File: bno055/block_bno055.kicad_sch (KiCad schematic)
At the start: 11 parts, among them U1 BNO055, Y1 NX3215SA-32.768K-STD-MUA-14

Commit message: [Rushil] added block of ds3231_rtc
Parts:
- added R2, R5: 10k, Resistor_SMD:R_0603_1608Metric, symbol Library:R
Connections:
- net +3V3: now also R2.1, R5.1
- net SCL: now also R2.2
- net SDA: now also R5.2

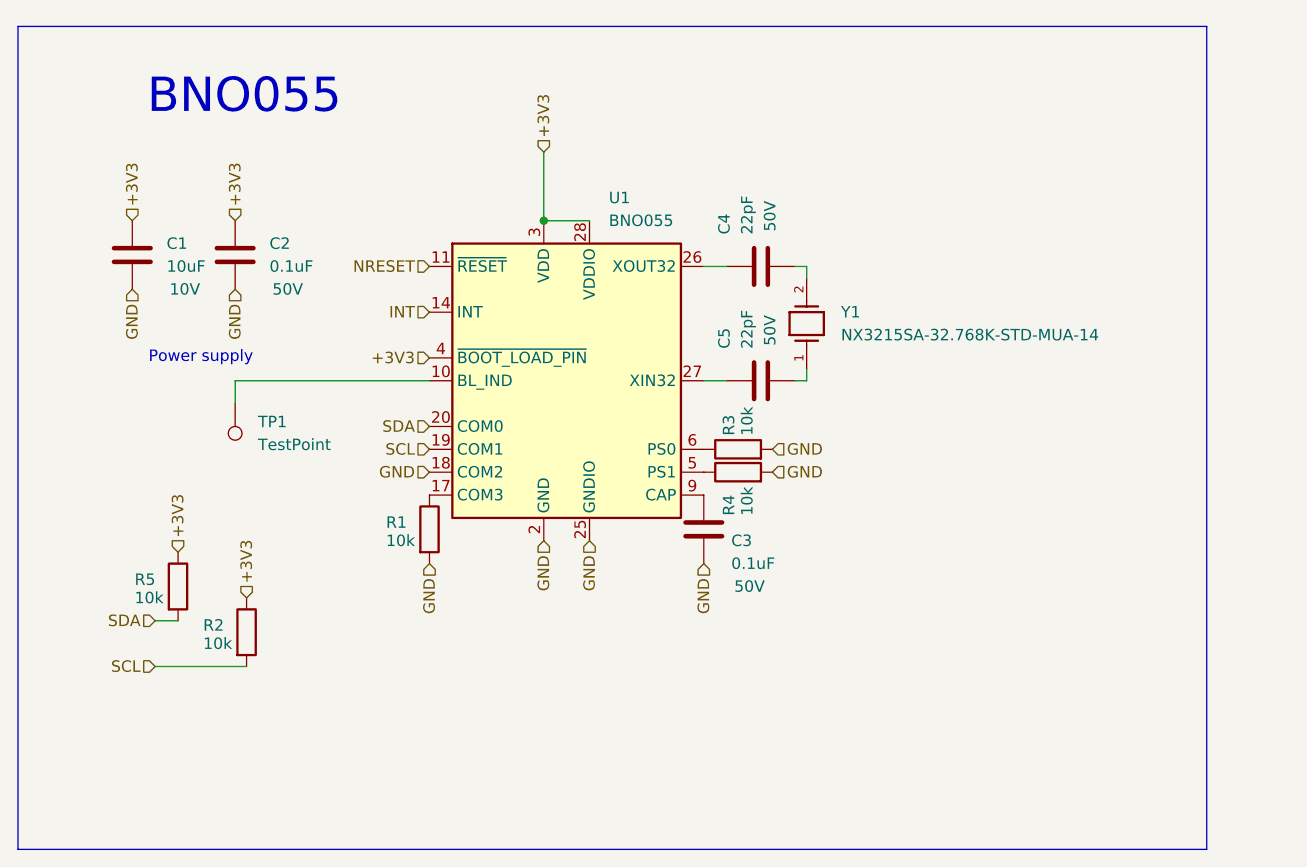
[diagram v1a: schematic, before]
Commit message: [Rushil] corrected pcb added information on both schematic and pcb user drawing correct circuit of bno055
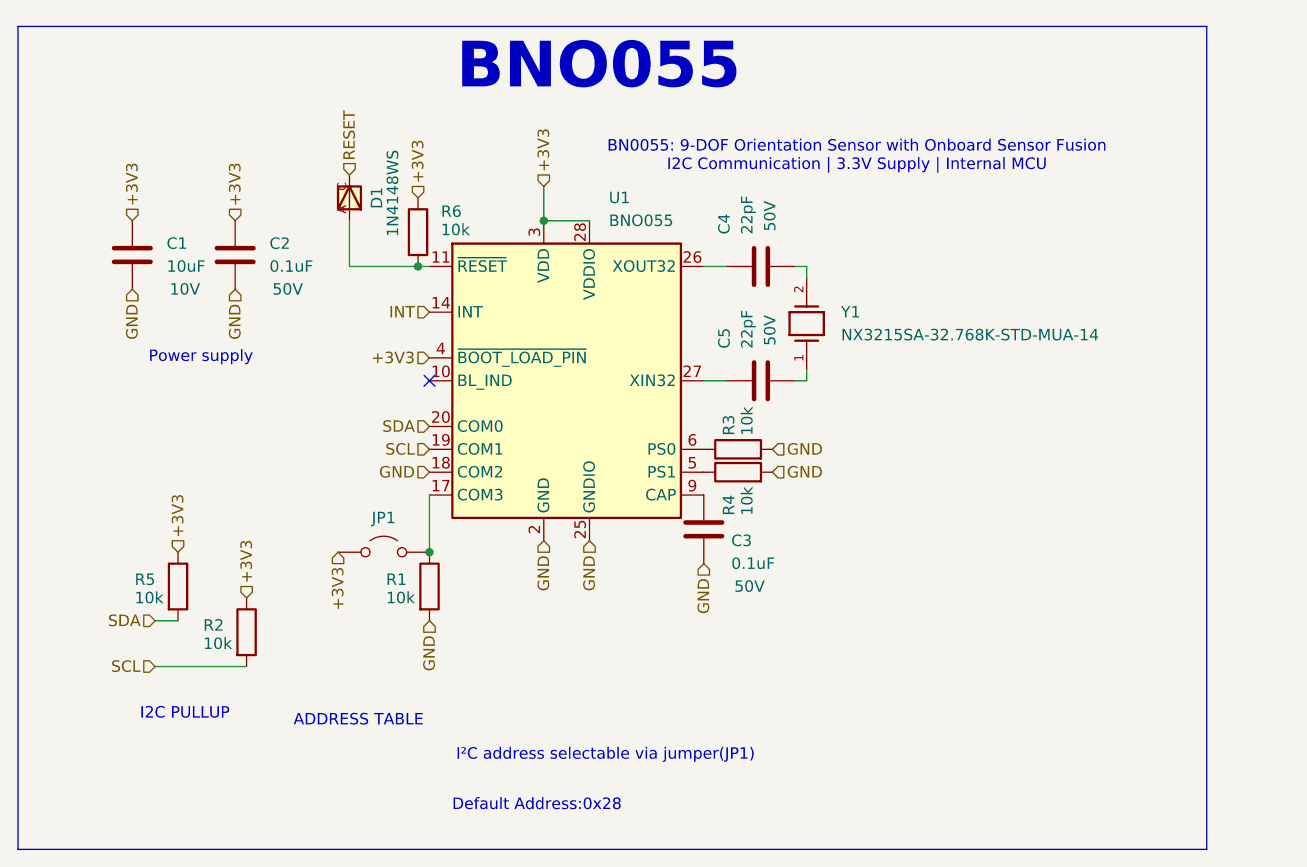
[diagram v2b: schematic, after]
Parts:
- removed TP1: TestPoint, TestPoint:TestPoint_Pad_D1.5mm, symbol Library:TestPoint
- added D1: 1N4148WS, 1N4148WS:SOD323, symbol Library:1N4148WS
- added JP1: Jumper_2_Open, Jumper:SolderJumper-2_P1.3mm_Open_RoundedPad1.0x1.5mm, symbol Library:Jumper_2_Open
- added R6: 10k, Resistor_SMD:R_0603_1608Metric, symbol Library:R
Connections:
- net +3V3: now also JP1.1 (A), R6.1
- net at R1.1, U1.17 (COM3): now also JP1.2 (B)
- net NRESET: no longer names the net of U1.11 (~{RESET})
- net NRESET: now also D1.A, R6.2
- new net RESET: D1.C
- no-connect marks 0 -> 1
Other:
- note added: "ADDRESS TABLE"
- note added: "BN0055: 9-DOF Orientation Sensor with Onboard Sensor Fusion I2C Communication | 3.3V Supply | Internal MCU"
- note added: "Default Address:0x28"
- note added: "I2C PULLUP"
- note added: "I²C address selectable via jumper(JP1)"
- moved on the sheet: R1

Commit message: [Rushil] added ams1117-3.3 block and did some clean up in schematic info part
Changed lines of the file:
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@@
 	(text "BN0055: 9-DOF Orientation Sensor with Onboard Sensor Fusion\nI2C Communication | 3.3V Supply | Internal MCU\n"
 		(exclude_from_sim no)
-		(at 180.848 67.818 0)
+		(at 155.194 67.818 0)
 		(effects
 			(font
 				(size 1.27 1.27)
 			)
+			(justify left)
 		)
 	)

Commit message: fixed BNO055
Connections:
- net +3V3 renamed 3V3
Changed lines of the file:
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@@
 	(text "Default Address:0x28\n"
 		(exclude_from_sim no)
-		(at 145.288 139.954 0)
+		(at 144.018 136.652 0)
 		(effects
 			(font
@@
 			(width 0)
 			(type default)
+		)
+	)
+	(table
+		(column_count 1)
+		(border
+			(external yes)
+			(header yes)
+			(stroke
+				(width 0)
+				(type solid)
+			)
+		)
+		(separators
+			(rows yes)
+			(cols yes)
+			(stroke
+				(width 0)
+				(type solid)
+			)
+		)
+		(column_widths 6.35)
+		(row_heights 2.54 2.54 2.54)
+		(cells
+			(table_cell "COM3"
+				(exclude_from_sim no)
+				(at 119.38 133.35 0)
+				(size 6.35 2.54)
+				(margins 0.9525 0.9525 0.9525 0.9525)
+				(span 1 1)
+				(fill
+					(type none)
+				)
+				(effects
+					(font
+						(size 1.27 1.27)
+					)
+					(justify left top)
+				)
+			)
+			(table_cell "HIGH"
+				(exclude_from_sim no)
+				(at 119.38 135.89 0)
+				(size 6.35 2.54)
+				(margins 0.9525 0.9525 0.9525 0.9525)
+				(span 1 1)
+				(fill
+					(type none)
+				)
+				(effects
+					(font
+						(size 1.27 1.27)
+					)
+					(justify left top)
+				)
+			)
+			(table_cell "LOW"
+				(exclude_from_sim no)
+				(at 119.38 138.43 0)
+				(size 6.35 2.54)
+				(margins 0.9525 0.9525 0.9525 0.9525)
+				(span 1 1)
+				(fill
+					(type none)
+				)
+				(effects
+					(font
+						(size 1.27 1.27)
+					)
+					(justify left top)
+				)
+			)
 		)
 	)
@@
 		)
 	)
-	(table
-		(column_count 1)
-		(border
-			(external yes)
-			(header yes)
-			(stroke
-				(width 0)
-				(type solid)
-			)
-		)
-		(separators
-			(rows yes)
-			(cols yes)
-			(stroke
-				(width 0)
-				(type solid)
-			)
-		)
-		(column_widths 6.35)
-		(row_heights 2.54 2.54 2.54)
-		(cells
-			(table_cell "COM3"
-				(exclude_from_sim no)
-				(at 119.38 133.35 0)
-				(size 6.35 2.54)
-				(margins 0.9525 0.9525 0.9525 0.9525)
-				(span 1 1)
-				(fill
-					(type none)
-				)
-				(effects
-					(font
-						(size 1.27 1.27)
-					)
-					(justify left top)
-				)
-			)
-			(table_cell "HIGH"
-				(exclude_from_sim no)
-				(at 119.38 135.89 0)
-				(size 6.35 2.54)
-				(margins 0.9525 0.9525 0.9525 0.9525)
-				(span 1 1)
-				(fill
-					(type none)
-				)
-				(effects
-					(font
-						(size 1.27 1.27)
-					)
-					(justify left top)
-				)
-			)
-			(table_cell "LOW"
-				(exclude_from_sim no)
-				(at 119.38 138.43 0)
-				(size 6.35 2.54)
-				(margins 0.9525 0.9525 0.9525 0.9525)
-				(span 1 1)
-				(fill
-					(type none)
-				)
-				(effects
-					(font
-						(size 1.27 1.27)
-					)
-					(justify left top)
-				)
-			)
-		)
-	)
 	(hierarchical_label "RESET"
 		(shape input)
@@
 		)
 	)
-	(hierarchical_label "+3V3"
+	(hierarchical_label "3V3"
 		(shape input)
 		(at 111.76 74.93 90)
@@
 		)
 	)
-	(hierarchical_label "+3V3"
+	(hierarchical_label "3V3"
 		(shape input)
 		(at 146.05 71.12 90)
@@
 		)
 	)
-	(hierarchical_label "+3V3"
+	(hierarchical_label "3V3"
 		(shape input)
 		(at 133.35 90.17 180)
@@
 		)
 	)
-	(hierarchical_label "+3V3"
+	(hierarchical_label "3V3"
 		(shape input)
 		(at 105.41 111.76 90)
@@
 		)
 	)
-	(hierarchical_label "+3V3"
+	(hierarchical_label "3V3"
 		(shape input)
 		(at 132.08 72.39 90)
@@
 		)
 	)
-	(hierarchical_label "+3V3"
+	(hierarchical_label "3V3"
 		(shape input)
 		(at 113.03 116.84 90)
@@
 		)
 	)
-	(hierarchical_label "+3V3"
+	(hierarchical_label "3V3"
 		(shape input)
 		(at 123.19 111.76 270)
@@
 		)
 	)
-	(hierarchical_label "+3V3"
+	(hierarchical_label "3V3"
 		(shape input)
 		(at 100.33 74.93 90)
